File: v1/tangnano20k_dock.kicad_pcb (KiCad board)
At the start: 2 copper layers, 122.6 x 57.2 mm, 54 parts, among them J1 Mini-DIN-6, J2 Conn_01x02, J3 DB15_Female_HighDensity_Mount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, J4 DB9_Male_MountingHoles, J5 Conn_02x10_Odd_Even, J6 Conn_02x10_Odd_Even, J7 RCA, J8 FCR684205T, J9 AudioJack3, U1 TXS0104E, U2 TangNano20K, U3 CS4354

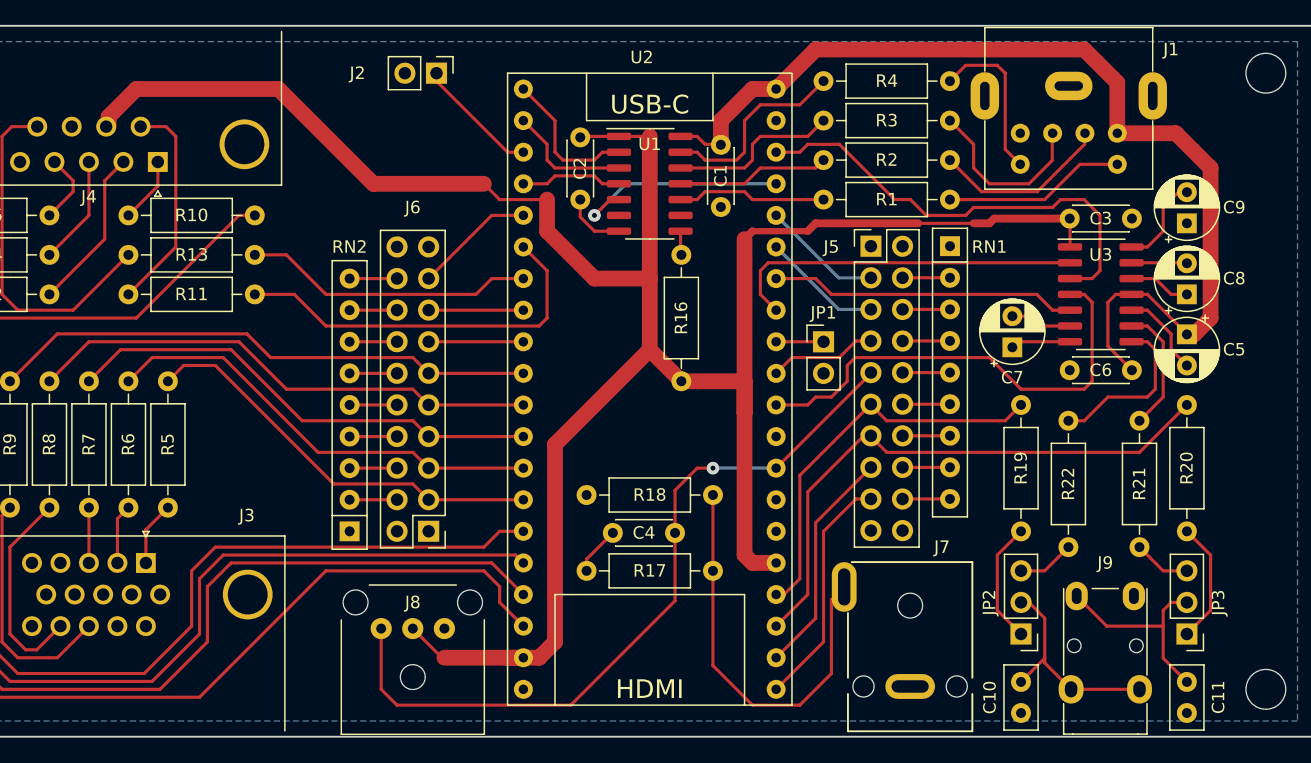
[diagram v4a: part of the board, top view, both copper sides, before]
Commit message: Silk screen only
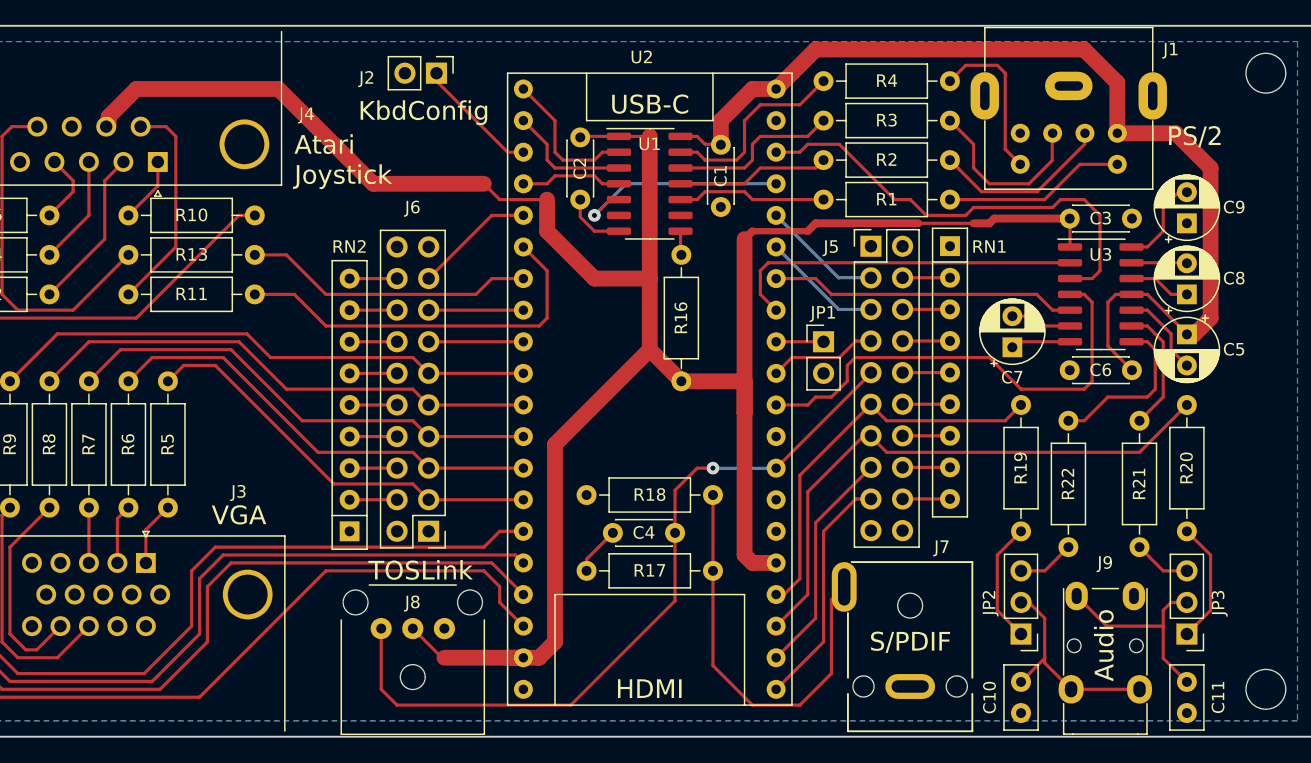
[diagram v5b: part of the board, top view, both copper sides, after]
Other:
- board text added: "Atari Joystick"
- board text added: "Audio"
- board text added: "KbdConfig"
- board text added: "PS/2"
- board text added: "S/PDIF"
- board text added: "TOSLink"
- board text added: "VGA"
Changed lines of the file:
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@@
     (property "Sheetname" "")
     (attr through_hole)
-    (fp_text reference "J3" (at 8.12 -3.81) (layer "F.SilkS")
+    (fp_text reference "J3" (at 7.485 -5.715) (layer "F.SilkS")
       (effects (font (size 1 1) (thickness 0.15)))
     )
@@
     (property "Sheetname" "")
     (attr through_hole)
-    (fp_text reference "J2" (at 0 6.35 180) (layer "F.SilkS")
+    (fp_text reference "J2" (at 0.381 5.588 180) (layer "F.SilkS")
       (effects (font (size 1 1) (thickness 0.15)))
     )
@@
     (property "Sheetname" "")
     (attr through_hole)
-    (fp_text reference "J4" (at 5.54 -2.8) (layer "F.SilkS")
+    (fp_text reference "J4" (at -11.986 3.833) (layer "F.SilkS")
       (effects (font (size 1 1) (thickness 0.15)))
     )
@@
   (gr_line (start 91.44 146.05) (end 91.44 88.9) (layer "Edge.Cuts") (width 0.15))
   (gr_line (start 213.995 88.9) (end 213.995 146.05) (layer "Edge.Cuts") (width 0.15))
+  (gr_text "KbdConfig" (at 142.494 95.758) (layer "F.SilkS")
+    (effects (font (size 1.5 1.5) (thickness 0.2)))
+  )
+  (gr_text "S/PDIF" (at 181.61 138.43) (layer "F.SilkS")
+    (effects (font (size 1.5 1.5) (thickness 0.2)))
+  )
+  (gr_text "Atari\nJoystick" (at 132.08 99.695) (layer "F.SilkS")
+    (effects (font (size 1.5 1.5) (thickness 0.2)) (justify left))
+  )
+  (gr_text "TOSLink" (at 142.24 132.715) (layer "F.SilkS")
+    (effects (font (size 1.5 1.5) (thickness 0.2)))
+  )
+  (gr_text "PS/2" (at 204.47 97.79) (layer "F.SilkS")
+    (effects (font (size 1.5 1.5) (thickness 0.2)))
+  )
+  (gr_text "Audio" (at 197.231 138.684 90) (layer "F.SilkS")
+    (effects (font (size 1.5 1.5) (thickness 0.2)))
+  )
+  (gr_text "VGA" (at 127.635 128.27) (layer "F.SilkS")
+    (effects (font (size 1.5 1.5) (thickness 0.2)))
+  )
   (segment (start 155.067 104.267) (end 155.067 102.87) (width 0.254) (layer "F.Cu") (net 1))
   (segment (start 202.565 113.665) (end 202.565 114.935) (width 0.254) (layer "F.Cu") (net 1))

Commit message: Minor changes
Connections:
- R8 pad 2: /GPIO3 -> /GPIO4
- R9 pad 2: /GPIO4 -> /GPIO3
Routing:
- net /GPIO3: track 41.5 -> 47.0 mm
- net /GPIO4: track 44.2 -> 41.4 mm
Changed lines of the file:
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@@
       (net 24 "/VGA_VS") (pintype "passive"))
     (pad "2" thru_hole oval (at 10.16 0 90) (size 1.6 1.6) (drill 0.8) (layers *.Cu *.Mask)
-      (net 49 "/GPIO3") (pintype "passive"))
+      (net 47 "/GPIO4") (pintype "passive"))
     (model "${KICAD6_3DMODEL_DIR}/Resistor_THT.3dshapes/R_Axial_DIN0207_L6.3mm_D2.5mm_P10.16mm_Horizontal.wrl"
       (offset (xyz 0 0 0))
@@
       (net 23 "/VGA_HS") (pintype "passive"))
     (pad "2" thru_hole oval (at 10.16 0 90) (size 1.6 1.6) (drill 0.8) (layers *.Cu *.Mask)
-      (net 47 "/GPIO4") (pintype "passive"))
+      (net 49 "/GPIO3") (pintype "passive"))
     (model "${KICAD6_3DMODEL_DIR}/Resistor_THT.3dshapes/R_Axial_DIN0207_L6.3mm_D2.5mm_P10.16mm_Horizontal.wrl"
       (offset (xyz 0 0 0))
@@
   (segment (start 142.875 114.3) (end 150.495 114.3) (width 0.254) (layer "F.Cu") (net 45))
   (segment (start 136.525 127) (end 140.335 127) (width 0.254) (layer "F.Cu") (net 46))
-  (segment (start 130.175 115.57) (end 128.27 113.665) (width 0.254) (layer "F.Cu") (net 47))
+  (segment (start 112.395 116.84) (end 112.395 117.475) (width 0.254) (layer "F.Cu") (net 47))
+  (segment (start 128.27 113.665) (end 115.57 113.665) (width 0.254) (layer "F.Cu") (net 47))
   (segment (start 142.875 116.84) (end 150.495 116.84) (width 0.254) (layer "F.Cu") (net 47))
-  (segment (start 142.88 116.835) (end 141.615 115.57) (width 0.254) (layer "F.Cu") (net 47))
-  (segment (start 113.03 113.665) (end 109.22 117.475) (width 0.254) (layer "F.Cu") (net 47))
+  (segment (start 130.175 115.57) (end 128.27 113.665) (width 0.254) (layer "F.Cu") (net 47))
   (segment (start 141.615 115.57) (end 130.175 115.57) (width 0.254) (layer "F.Cu") (net 47))
-  (segment (start 128.27 113.665) (end 113.03 113.665) (width 0.254) (layer "F.Cu") (net 47))
+  (segment (start 115.57 113.665) (end 112.395 116.84) (width 0.254) (layer "F.Cu") (net 47))
+  (segment (start 142.88 116.835) (end 141.615 115.57) (width 0.254) (layer "F.Cu") (net 47))
   (segment (start 136.525 124.46) (end 140.335 124.46) (width 0.254) (layer "F.Cu") (net 48))
+  (segment (start 141.605 118.11) (end 131.445 118.11) (width 0.254) (layer "F.Cu") (net 49))
   (segment (start 142.875 119.38) (end 150.495 119.38) (width 0.254) (layer "F.Cu") (net 49))
-  (segment (start 115.57 114.3) (end 112.395 117.475) (width 0.254) (layer "F.Cu") (net 49))
+  (segment (start 116.84 114.3) (end 113.974506 117.165494) (width 0.254) (layer "F.Cu") (net 49))
   (segment (start 131.445 118.11) (end 127.635 114.3) (width 0.254) (layer "F.Cu") (net 49))
+  (segment (start 113.974506 118.435494) (end 113.03 119.38) (width 0.254) (layer "F.Cu") (net 49))
+  (segment (start 113.03 119.38) (end 111.125 119.38) (width 0.254) (layer "F.Cu") (net 49))
+  (segment (start 113.974506 117.165494) (end 113.974506 118.435494) (width 0.254) (layer "F.Cu") (net 49))
+  (segment (start 111.125 119.38) (end 109.22 117.475) (width 0.254) (layer "F.Cu") (net 49))
+  (segment (start 127.635 114.3) (end 116.84 114.3) (width 0.254) (layer "F.Cu") (net 49))
   (segment (start 142.87 119.375) (end 141.605 118.11) (width 0.254) (layer "F.Cu") (net 49))
-  (segment (start 141.605 118.11) (end 131.445 118.11) (width 0.254) (layer "F.Cu") (net 49))
-  (segment (start 127.635 114.3) (end 115.57 114.3) (width 0.254) (layer "F.Cu") (net 49))
   (segment (start 136.525 121.92) (end 140.335 121.92) (width 0.254) (layer "F.Cu") (net 50))
   (segment (start 142.875 121.92) (end 150.495 121.92) (width 0.254) (layer "F.Cu") (net 51))

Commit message: Start again, using 1206 SMT
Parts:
- removed the J5 at (178.4, 106.6)
- removed the J6 at (142.9, 129.5)
- removed the R10 at (118.7, 104.1)
- removed the R11 at (118.7, 110.5)
- removed the R5 at (121.9, 127.6)
- removed the R6 at (118.7, 127.6)
- removed the R7 at (115.6, 127.6)
- removed the R8 at (112.4, 127.6)
- removed the R9 at (109.2, 127.6)
- added C12: 47p, Capacitor_SMD:C_1206_3216Metric_Pad1.33x1.80mm_HandSolder, F.Cu at (129.2, 113.7)
- added C13: 47p, Capacitor_SMD:C_1206_3216Metric_Pad1.33x1.80mm_HandSolder, F.Cu at (120.0, 113.7)
- added C14: 47p, Capacitor_SMD:C_1206_3216Metric_Pad1.33x1.80mm_HandSolder, F.Cu at (111.1, 113.7)
- added C15: 120p, Capacitor_SMD:C_1206_3216Metric_Pad1.33x1.80mm_HandSolder, F.Cu at (129.2, 118.7)
- added C16: 120p, Capacitor_SMD:C_1206_3216Metric_Pad1.33x1.80mm_HandSolder, F.Cu at (120.0, 118.7)
- added C17: 120p, Capacitor_SMD:C_1206_3216Metric_Pad1.33x1.80mm_HandSolder, F.Cu at (111.1, 118.7)
- added C18: 47p, Capacitor_SMD:C_1206_3216Metric_Pad1.33x1.80mm_HandSolder, F.Cu at (129.2, 123.8)
- added C19: 47p, Capacitor_SMD:C_1206_3216Metric_Pad1.33x1.80mm_HandSolder, F.Cu at (120.0, 123.8)
- added C20: 47p, Capacitor_SMD:C_1206_3216Metric_Pad1.33x1.80mm_HandSolder, F.Cu at (111.1, 123.8)
- added J10: DB9_Male_MountingHoles, Connector_Dsub:DSUB-9_Male_Horizontal_P2.77x2.84mm_EdgePinOffset7.70mm_Housed_MountingHolesOffset9.12mm, F.Cu at (105.4, 85.1)
- added J11: DB9_Male_MountingHoles, Connector_Dsub:DSUB-9_Male_Horizontal_P2.77x2.84mm_EdgePinOffset7.70mm_Housed_MountingHolesOffset9.12mm, F.Cu at (139.1, 85.1)
- added J12: Conn_02x06_Odd_Even, Connector_PinHeader_2.54mm:PinHeader_2x06_P2.54mm_Vertical, F.Cu at (115.1, 91.1)
- added J2: 2x20 Pin Male, Connector_PinHeader_2.54mm:PinHeader_2x20_P2.54mm_Vertical, F.Cu at (154.3, 96.5)
- added J9: DB15_Female_HighDensity_MountingHoles, TangNano20k:DSUB-15-HD_Female_Horizontal_P2.29x1.98mm_EdgePinOffset8.35mm_Housed_MountingHolesOffset10.89mm, F.Cu at (120.5, 132.0)
- added L1: 3u3, Inductor_SMD:L_1206_3216Metric_Pad1.42x1.75mm_HandSolder, F.Cu at (125.1, 116.2)
- added L2: 3u3, Inductor_SMD:L_1206_3216Metric_Pad1.42x1.75mm_HandSolder, F.Cu at (116.2, 116.2)
- added L3: 3u3, Inductor_SMD:L_1206_3216Metric_Pad1.42x1.75mm_HandSolder, F.Cu at (107.3, 116.2)
- added L4: 3u3, Inductor_SMD:L_1206_3216Metric_Pad1.42x1.75mm_HandSolder, F.Cu at (125.1, 121.3)
- added L5: 3u3, Inductor_SMD:L_1206_3216Metric_Pad1.42x1.75mm_HandSolder, F.Cu at (116.2, 121.3)
- added L6: 3u3, Inductor_SMD:L_1206_3216Metric_Pad1.42x1.75mm_HandSolder, F.Cu at (107.3, 121.3)
- added R16: 100, Resistor_SMD:R_1206_3216Metric_Pad1.30x1.75mm_HandSolder, F.Cu at (101.6, 119.4)
- added R17: 180, Resistor_SMD:R_1206_3216Metric_Pad1.30x1.75mm_HandSolder, F.Cu at (125.1, 111.1)
- added R18: 180, Resistor_SMD:R_1206_3216Metric_Pad1.30x1.75mm_HandSolder, F.Cu at (116.2, 111.1)
- added R19: 180, Resistor_SMD:R_1206_3216Metric_Pad1.30x1.75mm_HandSolder, F.Cu at (107.3, 111.1)
- added R20: 100, Resistor_SMD:R_1206_3216Metric_Pad1.30x1.75mm_HandSolder, F.Cu at (125.1, 126.4)
- added R21: 100, Resistor_SMD:R_1206_3216Metric_Pad1.30x1.75mm_HandSolder, F.Cu at (116.2, 126.4)
- added R22: 100, Resistor_SMD:R_1206_3216Metric_Pad1.30x1.75mm_HandSolder, F.Cu at (107.3, 126.4)
- added U4: 74LV165A, Package_SO:SOIC-16_3.9x9.9mm_P1.27mm, F.Cu at (99.9, 93.6)
- added U5: 74LV165A, Package_SO:SOIC-16_3.9x9.9mm_P1.27mm, F.Cu at (132.9, 94.3)
- C1, C2, C6: footprint Capacitor_THT:C_Disc_D4.3mm_W1.9mm_P5.00mm -> Capacitor_SMD:C_1206_3216Metric_Pad1.33x1.80mm_HandSolder
- C10, C11: value 2n2 -> 4n7; footprint Capacitor_THT:C_Disc_D5.0mm_W2.5mm_P2.50mm -> Capacitor_SMD:C_1206_3216Metric_Pad1.33x1.80mm_HandSolder
- C3: renamed from C4; footprint Capacitor_THT:C_Disc_D4.3mm_W1.9mm_P5.00mm -> Capacitor_SMD:C_1206_3216Metric_Pad1.33x1.80mm_HandSolder
- C4: renamed from C3; footprint Capacitor_THT:C_Disc_D4.3mm_W1.9mm_P5.00mm -> Capacitor_SMD:C_1206_3216Metric_Pad1.33x1.80mm_HandSolder
- C5, C7, C8, C9: footprint Capacitor_THT:CP_Radial_D5.0mm_P2.50mm -> Capacitor_SMD:C_1206_3216Metric_Pad1.33x1.80mm_HandSolder
- J3: value DB15_Female_HighDensity_MountingHoles -> 2x20 Pin Female; footprint TangNano20k:DSUB-15-HD_Female_Horizontal_P2.29x1.98mm_EdgePinOffset8.35mm_Housed_MountingHolesOffset10.89mm -> Connector_PinSocket_2.54mm:PinSocket_2x20_P2.54mm_Vertical
- J4: value DB9_Male_MountingHoles -> Conn_01x03_Male; footprint Connector_Dsub:DSUB-9_Male_Horizontal_P2.77x2.84mm_EdgePinOffset7.70mm_Housed_MountingHolesOffset9.12mm -> Connector_PinHeader_2.54mm:PinHeader_1x03_P2.54mm_Vertical
- R1: renamed from R4; footprint Resistor_THT:R_Axial_DIN0207_L6.3mm_D2.5mm_P10.16mm_Horizontal -> Resistor_SMD:R_1206_3216Metric_Pad1.30x1.75mm_HandSolder
- R10: renamed from R22; footprint Resistor_THT:R_Axial_DIN0207_L6.3mm_D2.5mm_P10.16mm_Horizontal -> Resistor_SMD:R_1206_3216Metric_Pad1.30x1.75mm_HandSolder
- R11: renamed from R21; footprint Resistor_THT:R_Axial_DIN0207_L6.3mm_D2.5mm_P10.16mm_Horizontal -> Resistor_SMD:R_1206_3216Metric_Pad1.30x1.75mm_HandSolder
- R12, R13, R14: value 180 -> 330; footprint Resistor_THT:R_Axial_DIN0207_L6.3mm_D2.5mm_P10.16mm_Horizontal -> Resistor_SMD:R_1206_3216Metric_Pad1.30x1.75mm_HandSolder
- R15: value 180 -> 100; footprint Resistor_THT:R_Axial_DIN0207_L6.3mm_D2.5mm_P10.16mm_Horizontal -> Resistor_SMD:R_1206_3216Metric_Pad1.30x1.75mm_HandSolder
- R2: renamed from R3; footprint Resistor_THT:R_Axial_DIN0207_L6.3mm_D2.5mm_P10.16mm_Horizontal -> Resistor_SMD:R_1206_3216Metric_Pad1.30x1.75mm_HandSolder
- R3: renamed from R2; footprint Resistor_THT:R_Axial_DIN0207_L6.3mm_D2.5mm_P10.16mm_Horizontal -> Resistor_SMD:R_1206_3216Metric_Pad1.30x1.75mm_HandSolder
- R4: renamed from R1; footprint Resistor_THT:R_Axial_DIN0207_L6.3mm_D2.5mm_P10.16mm_Horizontal -> Resistor_SMD:R_1206_3216Metric_Pad1.30x1.75mm_HandSolder
- R5: renamed from R16; footprint Resistor_THT:R_Axial_DIN0207_L6.3mm_D2.5mm_P10.16mm_Horizontal -> Resistor_SMD:R_1206_3216Metric_Pad1.30x1.75mm_HandSolder
- R6: renamed from R17; footprint Resistor_THT:R_Axial_DIN0207_L6.3mm_D2.5mm_P10.16mm_Horizontal -> Resistor_SMD:R_1206_3216Metric_Pad1.30x1.75mm_HandSolder
- R7: renamed from R20; value 6K8 -> 3K3; footprint Resistor_THT:R_Axial_DIN0207_L6.3mm_D2.5mm_P10.16mm_Horizontal -> Resistor_SMD:R_1206_3216Metric_Pad1.30x1.75mm_HandSolder
- R8: renamed from R19; footprint Resistor_THT:R_Axial_DIN0207_L6.3mm_D2.5mm_P10.16mm_Horizontal -> Resistor_SMD:R_1206_3216Metric_Pad1.30x1.75mm_HandSolder
- R9: renamed from R18; footprint Resistor_THT:R_Axial_DIN0207_L6.3mm_D2.5mm_P10.16mm_Horizontal -> Resistor_SMD:R_1206_3216Metric_Pad1.30x1.75mm_HandSolder
- moved H4 166.1 mm to (46.4, 114.9)
- moved H2 165.1 mm to (45.7, 106.7)
- moved R12 121.4 mm to (211.4, 180.8), turned to 0 degrees
- moved R14 119.5 mm to (211.4, 174.2), turned to 0 degrees
- moved R13 116.3 mm to (211.4, 177.5)
- moved RN1 95.9 mm to (89.0, 100.6), turned to 0 degrees
- moved J7 89.0 mm to (224.8, 168.9)
- moved J4 83.1 mm to (204.0, 105.4), turned to 0 degrees
- moved H3 66.9 mm to (46.4, 96.5)
- moved J6 65.9 mm to (242.6, 167.0)
- moved R1 65.3 mm to (247.0, 73.7)
- moved R2 65.3 mm to (247.0, 76.8)
- moved R3 65.3 mm to (247.0, 80.0)
- moved R4 65.3 mm to (247.0, 83.2)
- moved R5 63.9 mm to (217.2, 83.2)
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- renumbered J2 to J5, J7 to J6, J8 to J7, J9 to J8, JP3 to JP2, JP2 to JP3
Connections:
- C3 pad 1: /GPIO11 -> /SPDIF
- J3 pad 1: /VGA_R -> unconnected-(J3-Pad1)
- J3 pad 10: GND -> /SerialRx
- J3 pad 11: unconnected-(J3-Pad11) -> /LED4
- J3 pad 12: unconnected-(J3-Pad12) -> /LED3
- J3 pad 13: /VGA_HS -> /LED0
- J3 pad 14: /VGA_VS -> GND
- J3 pad 15: unconnected-(J3-Pad15) -> /VGA_B
- J3 pad 2: /VGA_G -> +5V
- J3 pad 3: /VGA_B -> /LED1
- J3 pad 4: unconnected-(J3-Pad4) -> +5V
- J3 pad 5: GND -> /LED2
- J3 pad 7: GND -> /PWM_R
- J3 pad 8: GND -> /SerialTx
- J3 pad 9: unconnected-(J3-Pad9) -> GND
- J4 pad 1: /JS_1 -> GND
- J4 pad 2: /JS_2 -> /SerialTx
- J4 pad 3: /JS_3 -> /SerialRx
- J7 pad 3: /GPIO11 -> /SPDIF
- JP2 pad 2: Net-(C11-Pad2) -> Net-(C10-Pad2)
- JP2 pad 3: Net-(JP3-Pad3) -> Net-(JP2-Pad3)
- JP3 pad 2: Net-(C10-Pad2) -> Net-(C11-Pad2)
- JP3 pad 3: Net-(JP2-Pad3) -> Net-(JP3-Pad3)
- R12 pad 1: /JS_2 -> /VGA/VGA_R_n
- R12 pad 2: /JS_DOWN -> GND
- R13 pad 1: /JS_9 -> /VGA/VGA_G_n
- R13 pad 2: /JS_FIRE2 -> GND
- R14 pad 1: /JS_3 -> /VGA/VGA_B_n
- R14 pad 2: /JS_LEFT -> GND
- R15 pad 1: /JS_4 -> /VGA/VGA_VS
- R15 pad 2: /JS_RIGHT -> Net-(J9-Pad14)
- R7 pad 1: /GPIO13 -> /PWM_R
- R8 pad 1: /GPIO12 -> /PWM_L
- RN1 pad 1: GND -> +5V
- RN1 pad 2: Net-(J5-Pad4) -> /Joysticks/Cfg5
- RN1 pad 3: Net-(J5-Pad6) -> /Joysticks/Cfg4
- RN1 pad 4: Net-(J5-Pad8) -> /Joysticks/Cfg3
- RN1 pad 5: Net-(J5-Pad10) -> /Joysticks/JS2_Fire
- RN1 pad 6: Net-(J5-Pad12) -> /Joysticks/JS2_Right
- RN1 pad 7: Net-(J5-Pad14) -> /Joysticks/JS2_Left
- RN1 pad 8: Net-(J5-Pad16) -> /Joysticks/JS2_Down
- RN1 pad 9: Net-(J5-Pad18) -> /Joysticks/JS2_Up
- RN2 pad 1: GND -> +5V
- RN2 pad 2: Net-(J6-Pad4) -> /Joysticks/Cfg2
- RN2 pad 3: Net-(J6-Pad6) -> /Joysticks/Cfg1
- RN2 pad 4: Net-(J6-Pad8) -> /Joysticks/Cfg0
- RN2 pad 5: Net-(J6-Pad10) -> /Joysticks/JS1_Fire
- RN2 pad 6: Net-(J6-Pad12) -> /Joysticks/JS1_Right
- RN2 pad 7: Net-(J6-Pad14) -> /Joysticks/JS1_Left
- RN2 pad 8: Net-(J6-Pad16) -> /Joysticks/JS1_Down
- RN2 pad 9: Net-(J6-Pad18) -> /Joysticks/JS1_Up
- U2 pad 10: /GPIO4 -> /VGA_G
- U2 pad 11: /GPIO3 -> /VGA_G_n
- U2 pad 12: /GPIO2 -> /VGA_B
- U2 pad 13: /GPIO1 -> /VGA_B_n
- U2 pad 14: /GPIO0 -> /VGA_VS
- U2 pad 15: /JS_UP -> /LED2
- U2 pad 16: /JS_LEFT -> /LED3
- U2 pad 17: /JS_DOWN -> /LED4
- U2 pad 18: /JS_RIGHT -> /LED5
- U2 pad 21: /GPIO15 -> unconnected-(U2-Pad21)
- U2 pad 22: /GPIO14 -> unconnected-(U2-Pad22)
- U2 pad 23: /GPIO13 -> /JS_Clk
- U2 pad 24: /GPIO12 -> /JS_Load_n
- U2 pad 28: /GPIO11 -> /SPDIF
- U2 pad 31: /GPIO10 -> /I2S_MCLK
- U2 pad 35: /GPIO9 -> /PWM_L
- U2 pad 36: /GPIO8 -> /PWM_R
- U2 pad 37: /LV_MSE_CLK -> /LV_MSE_DATA
- U2 pad 38: /I2S_MCLK -> /JS_Data
- U2 pad 4: /LV_MSE_DATA -> /LV_MSE_CLK
- U2 pad 5: /GPIO7 -> /VGA_HS
- U2 pad 6: /JS_FIRE1 -> /LED0
- U2 pad 7: /JS_FIRE2 -> /LED1
- U2 pad 8: /GPIO6 -> /VGA_R
- U2 pad 9: /GPIO5 -> /VGA_R_n
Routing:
- net +3.3V: track 185.0 -> 0.00 mm
- net /JS_UP: track 106.0 -> 0.00 mm
- net /JS_RIGHT: track 91.5 -> 0.00 mm
- net /JS_LEFT: track 84.9 -> 0.00 mm
- net /JS_DOWN: track 84.2 -> 0.00 mm
- net +5V: track 82.1 -> 0.00 mm
- net /GPIO11: track 61.0 -> 0.00 mm, vias 1 -> 0
- net /GPIO3: track 47.0 -> 0.00 mm
- net /GPIO13: track 45.7 -> 0.00 mm
- net /GPIO4: track 41.4 -> 0.00 mm
- net /GPIO2: track 38.9 -> 0.00 mm
- net /I2S_LRCLK: track 37.4 -> 0.00 mm
- net /I2S_MCLK: track 36.8 -> 0.00 mm
- net /GPIO1: track 36.2 -> 0.00 mm
- net /GPIO0: track 33.6 -> 0.00 mm
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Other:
- board size 122.6 x 57.2 mm -> 126.4 x 78.7 mm
- board text removed: "VGA"

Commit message: Work in progress
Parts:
- removed the J2 at (154.3, 96.5)
- added C21: 100n, Capacitor_SMD:C_1206_3216Metric_Pad1.33x1.80mm_HandSolder, F.Cu at (102.2, 95.2)
- added C22: 100n, Capacitor_SMD:C_1206_3216Metric_Pad1.33x1.80mm_HandSolder, F.Cu at (135.9, 95.2)
- added J3: Conn_01x20, Connector_PinHeader_2.54mm:PinHeader_1x20_P2.54mm_Vertical, F.Cu at (156.8, 94.0)
- added J9: Conn_02x06_Odd_Even, Connector_PinHeader_2.54mm:PinHeader_2x06_P2.54mm_Vertical, F.Cu at (150.5, 111.8)
- R8: value 6K8 -> 3K3
- moved H2 172.8 mm to (215.9, 76.8)
- moved H4 171.8 mm to (215.9, 142.9)
- moved J4 108.5 mm to (100.3, 137.2), turned to 180 degrees
- moved R12 96.4 mm to (143.5, 112.4), turned to 180 degrees
- moved R13 89.0 mm to (143.5, 120.0), turned to 180 degrees
- moved J7 84.7 mm to (146.1, 137.8)
- moved R14 82.4 mm to (143.5, 127.6), turned to 180 degrees
- moved H3 61.6 mm to (87.0, 142.9)
- moved R7 57.5 mm to (191.1, 106.7), turned to 180 degrees
- moved J6 54.8 mm to (193.7, 142.2)
- moved C9 54.5 mm to (194.9, 116.8), turned to 0 degrees
- moved R1 53.6 mm to (196.2, 90.8), turned to -90 degrees
- moved C4 52.0 mm to (194.9, 121.9), turned to 0 degrees
- moved R2 49.0 mm to (200.0, 90.8), turned to -90 degrees
- moved C8 48.9 mm to (199.0, 113.7), turned to 180 degrees
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- renumbered J9 to J10, J10 to J11, J11 to J12, J12 to J13, J3 to J2
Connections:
- J2 pad 11: /LED4 -> /LED2
- J2 pad 12: /LED3 -> /LED1
- J2 pad 15: /VGA_B -> /VGA_HS
- J2 pad 16: /VGA_B_n -> /VGA_VS
- J2 pad 18: /VGA_VS -> /VGA_B_n
- J2 pad 19: /VGA_G -> /VGA_B
- J2 pad 21: /VGA_R_n -> /VGA_G_n
- J2 pad 22: /VGA_HS -> /VGA_G
- J2 pad 23: /VGA_G_n -> /VGA_R_n
- J2 pad 3: /LED1 -> /LED5
- J2 pad 40: /LED5 -> /PWM_R
- J2 pad 5: /LED2 -> /LED4
- J2 pad 7: /PWM_R -> /LED3
- J6 pad 1: /SPDIF -> Net-(J6-Pad1)
- JP1 pad 1: Net-(JP1-Pad1) -> GND
- JP1 pad 2: GND -> Net-(JP1-Pad2)
- R12 pad 1: /VGA/VGA_R_n -> Net-(J9-Pad3)
- R13 pad 1: /VGA/VGA_G_n -> Net-(J9-Pad7)
- R14 pad 1: /VGA/VGA_B_n -> Net-(J9-Pad11)
- R15 pad 1: /VGA/VGA_VS -> /VGA_VS
- R16 pad 1: /VGA/VGA_HS -> /VGA_HS
- R17 pad 1: /VGA/VGA_R -> Net-(J9-Pad1)
- R18 pad 1: /VGA/VGA_G -> Net-(J9-Pad5)
- R19 pad 1: /VGA/VGA_B -> Net-(J9-Pad9)
- R6 pad 2: /SPDIF -> Net-(J6-Pad1)
- R7 pad 1: /PWM_R -> /RC_AUDIO_R
- R7 pad 2: /RC_AUDIO_R -> /PWM_R
- R8 pad 1: /PWM_L -> /RC_AUDIO_L
- R8 pad 2: /RC_AUDIO_L -> /PWM_L
- R9 pad 2: /SPDIF -> Net-(J6-Pad1)
- RN1 pad 2: /Joysticks/Cfg5 -> /Joysticks/JS2_Fire
- RN1 pad 3: /Joysticks/Cfg4 -> /Joysticks/JS2_Right
- RN1 pad 4: /Joysticks/Cfg3 -> /Joysticks/JS2_Left
- RN1 pad 5: /Joysticks/JS2_Fire -> /Joysticks/JS2_Down
- RN1 pad 6: /Joysticks/JS2_Right -> /Joysticks/JS2_Up
- RN1 pad 7: /Joysticks/JS2_Left -> /Joysticks/Cfg5
- RN1 pad 8: /Joysticks/JS2_Down -> /Joysticks/Cfg4
- RN1 pad 9: /Joysticks/JS2_Up -> /Joysticks/Cfg3
- U2 pad 32: Net-(JP1-Pad1) -> Net-(JP1-Pad2)
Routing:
- net +5V: track 0.00 -> 278.0 mm
- net +3.3V: track 0.00 -> 165.4 mm
- net /JS_Clk: track 0.00 -> 102.9 mm, vias 0 -> 1
- net GND: track 0.00 -> 101.5 mm, vias 0 -> 16
- net /JS_Load_n: track 0.00 -> 91.6 mm, vias 0 -> 1
- net /VGA_HS: track 5.08 -> 93.4 mm, vias 0 -> 2
- net /LED0: track 5.08 -> 90.0 mm, vias 0 -> 2
- net /LED1: track 5.08 -> 87.2 mm, vias 0 -> 2
- net /LED2: track 5.08 -> 85.9 mm
- net /LED3: track 5.08 -> 84.6 mm
- net /LED4: track 5.08 -> 83.9 mm
- net /LED5: track 5.08 -> 83.1 mm
- net /PWM_R: track 27.5 -> 104.2 mm
- net /PWM_L: track 27.5 -> 102.3 mm
- net /VGA_R_n: track 5.08 -> 72.7 mm
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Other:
- board size 126.4 x 78.7 mm -> 139.7 x 73.7 mm
- board text added: "Line Audio"
- board text removed: "Audio"
- board text removed: "KbdConfig"
